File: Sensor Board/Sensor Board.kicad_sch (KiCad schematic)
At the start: 32 parts, among them J1 Programming Header, J3 Micro_SD_Card, U1 PIC18F26K83, U3 SPX3819M5-L-3-3, U4 MCP2562, Y1 12MHz Crystal

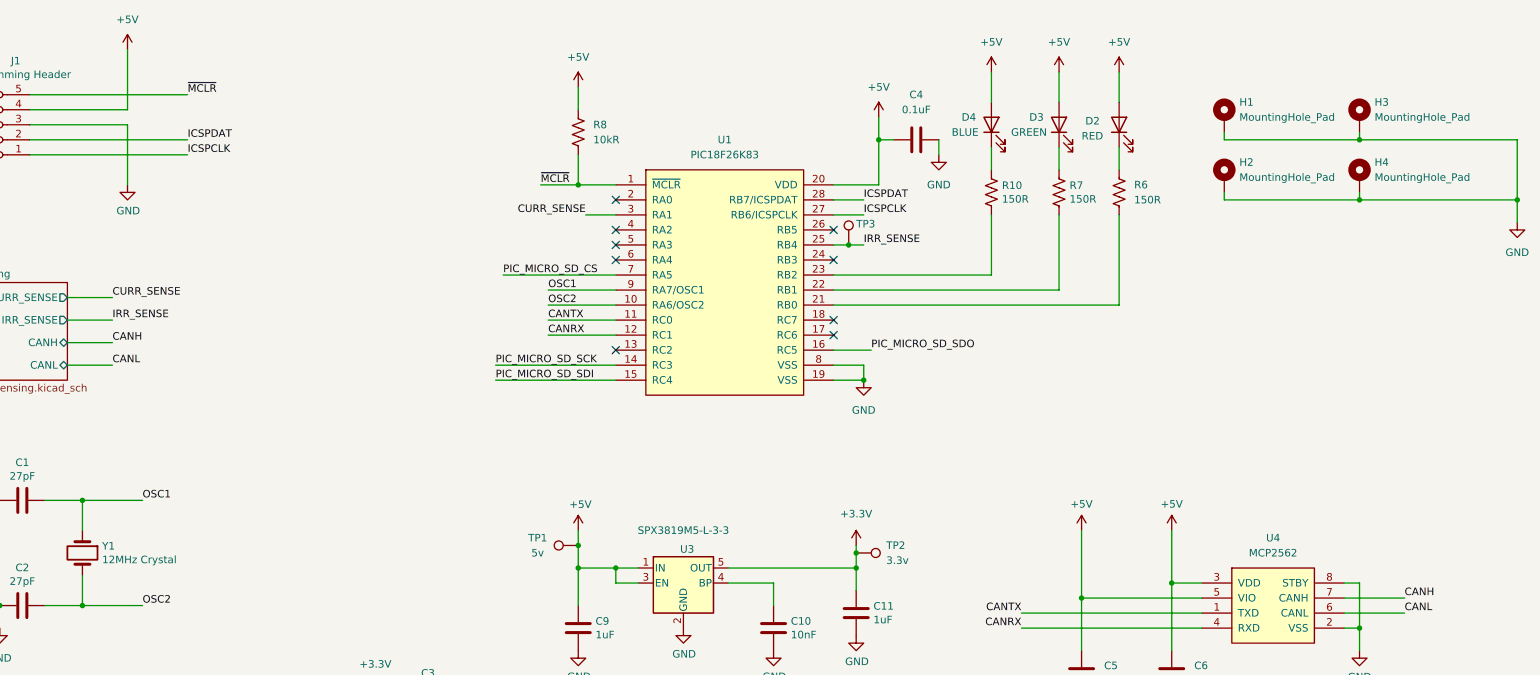
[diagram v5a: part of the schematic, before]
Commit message: Switch op amp
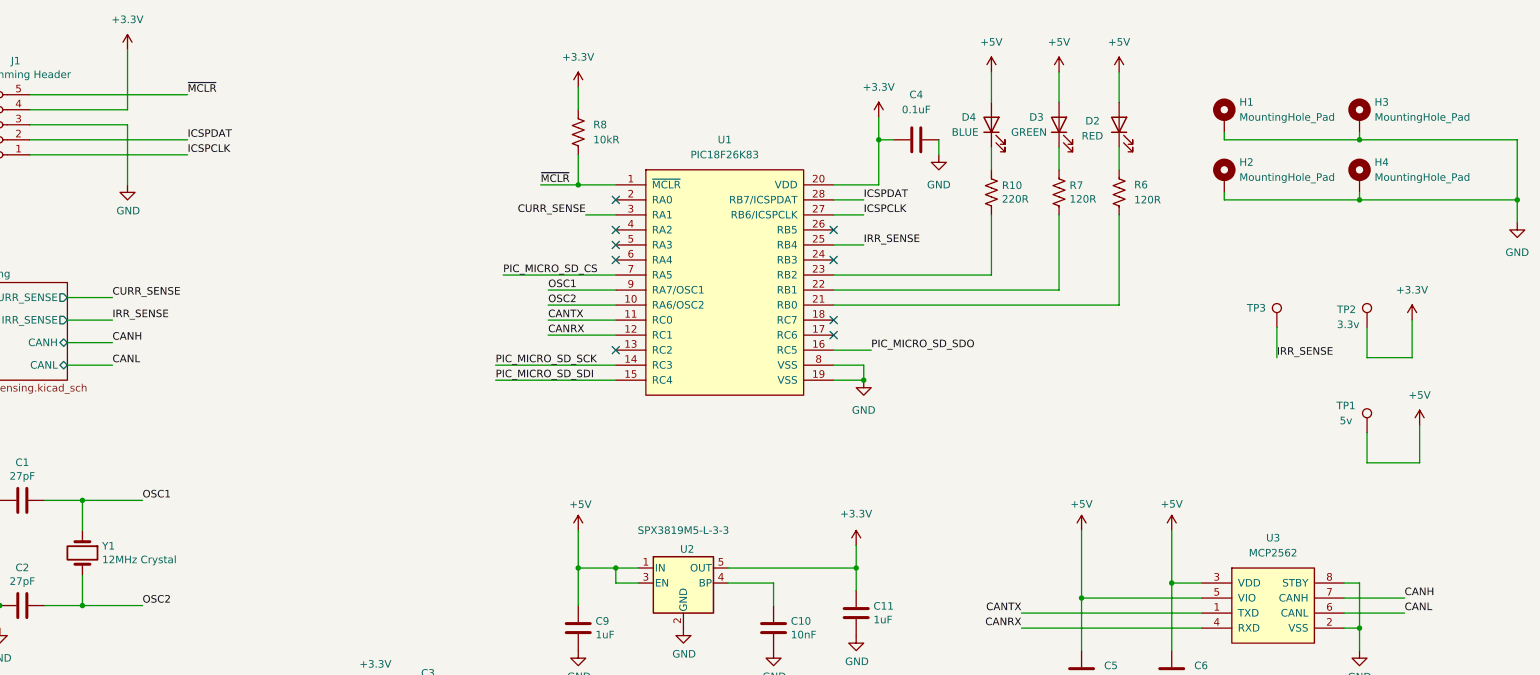
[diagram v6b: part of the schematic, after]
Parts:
- R10: value 150R -> 220R
- R6, R7: value 150R -> 120R
- U2: renamed from U3; footprint Package_TO_SOT_SMD:SOT-23-5 -> Package_TO_SOT_SMD:SOT-23-5_HandSoldering
- renumbered U4 to U3
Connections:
- net +3.3V: now also C4.1, J1.4 (Pin_4), R8.1, U1.20 (VDD)
- net +5V: no longer C4.1, J1.4 (Pin_4), R8.1, U1.20 (VDD)
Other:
- moved on the sheet: TP1, TP2, TP3

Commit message: Cooked another layout-Pranav
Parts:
- Y1: value 12MHz Crystal -> 12MHz Crystal
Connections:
- net CANRX: now also U1.25 (RB4); no longer U1.12 (RC1)
- net CANTX: now also U1.26 (RB5); no longer U1.11 (RC0)
- net CURR_SENSE: now also U1.4 (RA2); no longer U1.3 (RA1)
- net IRR_SENSE: now also U1.18 (RC7); no longer U1.25 (RB4)
- net PIC_MICRO_SD_CS: now also U1.21 (RB0); no longer U1.7 (RA5)
- net PIC_MICRO_SD_SCK: now also U1.23 (RB2); no longer U1.14 (RC3)
- net PIC_MICRO_SD_SDI: now also U1.24 (RB3); no longer U1.15 (RC4)
- net PIC_MICRO_SD_SDO: now also U1.22 (RB1); no longer U1.16 (RC5)
- net at U1.17 (RC6): now also R10.2
- net at R6.2: now also U1.15 (RC4); no longer U1.21 (RB0)
- net at R7.2: now also U1.16 (RC5); no longer U1.22 (RB1)
- no-connect marks 9 -> 8
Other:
- moved on the sheet: D2, R6
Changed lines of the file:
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@@
 	)
 	(no_connect
-		(at 162.56 73.66)
+		(at 125.73 78.74)
 	)
 	(no_connect
-		(at 125.73 60.96)
+		(at 125.73 53.34)
 	)
 	(no_connect
-		(at 162.56 71.12)
+		(at 125.73 60.96)
 	)
 	(no_connect
-		(at 125.73 50.8)
+		(at 125.73 73.66)
 	)
 	(no_connect
@@
 	)
 	(no_connect
-		(at 162.56 60.96)
-	)
-	(no_connect
-		(at 162.56 55.88)
+		(at 125.73 50.8)
 	)
 	(no_connect
@@
 	)
 	(no_connect
-		(at 125.73 55.88)
+		(at 125.73 71.12)
 	)
 	(wire
@@
 	(wire
 		(pts
-			(xy 200.66 29.21) (xy 200.66 34.29)
+			(xy 100.33 81.28) (xy 125.73 81.28)
 		)
 		(stroke
@@
 	(wire
 		(pts
-			(xy 120.65 53.34) (xy 125.73 53.34)
+			(xy 200.66 29.21) (xy 200.66 34.29)
 		)
 		(stroke
@@
 	(wire
 		(pts
-			(xy 210.82 29.21) (xy 210.82 34.29)
-		)
-		(stroke
-			(width 0)
-			(type default)
-		)
-	)
-	(wire
-		(pts
-			(xy 210.82 53.34) (xy 210.82 68.58)
+			(xy 100.33 27.94) (xy 100.33 33.02)
 		)
 		(stroke
@@
 	(wire
 		(pts
-			(xy 210.82 41.91) (xy 210.82 45.72)
+			(xy 100.33 40.64) (xy 100.33 44.45)
 		)
 		(stroke
@@
 	(wire
 		(pts
-			(xy 189.23 41.91) (xy 189.23 45.72)
+			(xy 200.66 53.34) (xy 200.66 76.2)
 		)
 		(stroke
@@
 	(wire
 		(pts
-			(xy 162.56 58.42) (xy 167.64 58.42)
+			(xy 189.23 41.91) (xy 189.23 45.72)
 		)
 		(stroke
@@
 	(wire
 		(pts
-			(xy 114.3 71.12) (xy 125.73 71.12)
-		)
-		(stroke
-			(width 0)
-			(type default)
-		)
-	)
-	(wire
-		(pts
 			(xy 85.09 134.62) (xy 85.09 138.43)
 		)
@@
 	(wire
 		(pts
-			(xy 162.56 66.04) (xy 200.66 66.04)
-		)
-		(stroke
-			(width 0)
-			(type default)
-		)
-	)
-	(wire
-		(pts
 			(xy 261.62 95.25) (xy 261.62 88.9)
 		)
@@
 	(wire
 		(pts
-			(xy 162.56 76.2) (xy 168.91 76.2)
-		)
-		(stroke
-			(width 0)
-			(type default)
-		)
-	)
-	(wire
-		(pts
 			(xy 125.73 115.57) (xy 125.73 113.03)
 		)
@@
 	(wire
 		(pts
-			(xy 105.41 81.28) (xy 125.73 81.28)
+			(xy 170.18 40.64) (xy 170.18 48.26)
 		)
 		(stroke
@@
 	(wire
 		(pts
-			(xy 170.18 40.64) (xy 170.18 48.26)
+			(xy 189.23 29.21) (xy 189.23 34.29)
 		)
 		(stroke
@@
 	(wire
 		(pts
-			(xy 189.23 29.21) (xy 189.23 34.29)
+			(xy 162.56 53.34) (xy 167.64 53.34)
 		)
 		(stroke
@@
 	(wire
 		(pts
-			(xy 162.56 53.34) (xy 167.64 53.34)
+			(xy 248.92 115.57) (xy 251.46 115.57)
 		)
 		(stroke
@@
 	(wire
 		(pts
-			(xy 248.92 115.57) (xy 251.46 115.57)
+			(xy 237.49 72.39) (xy 237.49 77.47)
 		)
 		(stroke
@@
 	(wire
 		(pts
-			(xy 237.49 72.39) (xy 237.49 77.47)
+			(xy 100.33 52.07) (xy 100.33 81.28)
 		)
 		(stroke
@@
 	(wire
 		(pts
-			(xy 200.66 53.34) (xy 200.66 66.04)
+			(xy 162.56 73.66) (xy 189.23 73.66)
 		)
 		(stroke
@@
 	(wire
 		(pts
-			(xy 189.23 53.34) (xy 189.23 63.5)
+			(xy 189.23 53.34) (xy 189.23 73.66)
 		)
 		(stroke
@@
 	(wire
 		(pts
-			(xy 114.3 73.66) (xy 125.73 73.66)
-		)
-		(stroke
-			(width 0)
-			(type default)
-		)
-	)
-	(wire
-		(pts
 			(xy 200.66 45.72) (xy 200.66 41.91)
 		)
@@
 	(wire
 		(pts
-			(xy 105.41 78.74) (xy 125.73 78.74)
-		)
-		(stroke
-			(width 0)
-			(type default)
-		)
-	)
-	(wire
-		(pts
 			(xy 144.78 113.03) (xy 166.37 113.03)
 		)
@@
 	(wire
 		(pts
-			(xy 21.59 119.38) (xy 21.59 123.19)
+			(xy 200.66 76.2) (xy 162.56 76.2)
 		)
 		(stroke
@@
 	(wire
 		(pts
-			(xy 172.72 40.64) (xy 170.18 40.64)
+			(xy 21.59 119.38) (xy 21.59 123.19)
 		)
 		(stroke
@@
 	(wire
 		(pts
-			(xy 106.68 63.5) (xy 125.73 63.5)
+			(xy 172.72 40.64) (xy 170.18 40.64)
 		)
 		(stroke
@@
 	(wire
 		(pts
-			(xy 162.56 68.58) (xy 210.82 68.58)
-		)
-		(stroke
-			(width 0)
-			(type default)
-		)
-	)
-	(wire
-		(pts
 			(xy 114.3 66.04) (xy 125.73 66.04)
 		)
@@
 	(wire
 		(pts
-			(xy 189.23 63.5) (xy 162.56 63.5)
-		)
-		(stroke
-			(width 0)
-			(type default)
-		)
-	)
-	(wire
-		(pts
 			(xy 48.26 181.61) (xy 48.26 161.29)
 		)
@@
 	)
 	(label "IRR_SENSE"
-		(at 167.64 58.42 0)
+		(at 162.56 71.12 0)
 		(fields_autoplaced yes)
 		(effects
@@
 	)
 	(label "CANTX"
-		(at 114.3 71.12 0)
+		(at 162.56 55.88 0)
 		(fields_autoplaced yes)
 		(effects
@@
 	)
 	(label "PIC_MICRO_SD_SCK"
-		(at 105.41 78.74 0)
+		(at 162.56 63.5 0)
 		(fields_autoplaced yes)
 		(effects
@@
 	)
 	(label "CANRX"
-		(at 114.3 73.66 0)
+		(at 162.56 58.42 0)
 		(fields_autoplaced yes)
 		(effects
@@
 	)
 	(label "PIC_MICRO_SD_SDO"
-		(at 168.91 76.2 0)
+		(at 162.56 66.04 0)
 		(fields_autoplaced yes)
 		(effects
@@
 	)
 	(label "PIC_MICRO_SD_SDI"
-		(at 105.41 81.28 0)
+		(at 162.56 60.96 0)
 		(fields_autoplaced yes)
 		(effects
@@
 	)
 	(label "PIC_MICRO_SD_CS"
-		(at 106.68 63.5 0)
+		(at 162.56 68.58 0)
 		(fields_autoplaced yes)
 		(effects
@@
 	)
 	(label "CURR_SENSE"
-		(at 120.65 53.34 180)
+		(at 125.73 55.88 180)
 		(fields_autoplaced yes)
 		(effects
@@
 			)
 		)
-		(property "Value" "12MHz Crystal "
+		(property "Value" "12MHz Crystal"
 			(at 38.8874 111.633 90)
 			(effects
@@
 		(lib_name "+5V_3")
 		(lib_id "power:+5V")
-		(at 210.82 29.21 0)
+		(at 100.33 27.94 0)
 		(unit 1)
 		(exclude_from_sim no)
@@
 		(fields_autoplaced yes)
 		(property "Reference" "#PWR06"
-			(at 210.82 33.02 0)
+			(at 100.33 31.75 0)
 			(effects
 				(font
@@
 		)
 		(property "Value" "+5V"
-			(at 210.82 24.13 0)
+			(at 100.33 22.86 0)
 			(effects
 				(font
@@
 		)
 		(property "Footprint" ""
-			(at 210.82 29.21 0)
+			(at 100.33 27.94 0)
 			(effects
 				(font
@@
 		)
 		(property "Datasheet" ""
-			(at 210.82 29.21 0)
+			(at 100.33 27.94 0)
 			(effects
 				(font
@@
 		)
 		(property "Description" "Power symbol creates a global label with name \"+5V\""
-			(at 210.82 29.21 0)
+			(at 100.33 27.94 0)
 			(effects
 				(font
@@
 	(symbol
 		(lib_id "Device:LED")
-		(at 210.82 38.1 90)
+		(at 100.33 36.83 90)
 		(unit 1)
 		(exclude_from_sim no)
@@
 		(dnp no)
 		(property "Reference" "D2"
-			(at 205.105 37.465 90)
+			(at 94.615 36.195 90)
 			(effects
 				(font
@@
 		)
 		(property "Value" "RED"
-			(at 204.47 40.005 90)
+			(at 93.98 38.735 90)
 			(effects
 				(font
@@
 		)
 		(property "Footprint" "LED_SMD:LED_1206_3216Metric_Pad1.42x1.75mm_HandSolder"
-			(at 210.82 38.1 0)
+			(at 100.33 36.83 0)
 			(effects
 				(font
@@
 		)
 		(property "Datasheet" "~"
-			(at 210.82 38.1 0)
+			(at 100.33 36.83 0)
 			(effects
 				(font
@@
 		)
 		(property "Description" ""
-			(at 210.82 38.1 0)
+			(at 100.33 36.83 0)
 			(effects
 				(font
@@
 		)
 		(property "DigiKey" "160-1457-1-ND"
-			(at 210.82 38.1 90)
+			(at 100.33 36.83 90)
 			(effects
 				(font
@@
 	(symbol
 		(lib_id "Device:R_US")
-		(at 210.82 49.53 0)
+		(at 100.33 48.26 0)
 		(unit 1)
 		(exclude_from_sim no)
@@
 		(fields_autoplaced yes)
 		(property "Reference" "R6"
-			(at 213.36 48.2599 0)
+			(at 102.87 46.9899 0)
 			(effects
 				(font
@@
 		)
 		(property "Value" "120R"
-			(at 213.36 50.7999 0)
+			(at 102.87 49.5299 0)
 			(effects
 				(font
@@
 		)
 		(property "Footprint" "Resistor_SMD:R_0805_2012Metric_Pad1.20x1.40mm_HandSolder"
-			(at 211.836 49.784 90)
+			(at 101.346 48.514 90)
 			(effects
 				(font
@@
 		)
 		(property "Datasheet" "~"
-			(at 210.82 49.53 0)
+			(at 100.33 48.26 0)
 			(effects
 				(font
@@
 		)
 		(property "Description" ""
-			(at 210.82 49.53 0)
+			(at 100.33 48.26 0)
 			(effects
 				(font
@@
 		)
 		(property "DigiKey" "738-RMCF0805FT160RCT-ND"
-			(at 210.82 49.53 0)
+			(at 100.33 48.26 0)
 			(effects
 				(font

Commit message: updated optics front end
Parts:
- removed C10: 10nF, Capacitor_SMD:C_0805_2012Metric_Pad1.18x1.45mm_HandSolder, symbol Device:C
- removed C11, C9: 1uF, Capacitor_SMD:C_0805_2012Metric_Pad1.18x1.45mm_HandSolder, symbol Device:C
- removed H1, H2, H3, H4: MountingHole_Pad, MountingHole:MountingHole_3.2mm_M3_DIN965_Pad, symbol Mechanical:MountingHole_Pad
- removed TP1: 5v, TestPoint:TestPoint_Pad_1.5x1.5mm, symbol Connector:TestPoint
- removed TP2: 3.3v, TestPoint:TestPoint_Pad_1.5x1.5mm, symbol Connector:TestPoint
- removed TP3: TestPoint, TestPoint:TestPoint_Pad_1.5x1.5mm, symbol Connector:TestPoint
- removed U2: SPX3819M5-L-3-3, Package_TO_SOT_SMD:SOT-23-5_HandSoldering, symbol Regulator_Linear:SPX3819M5-L-3-3
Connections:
- net +5V: no longer C5.2, U3.5 (VIO)
- net SCLK: now reaches U1.14 (RC3)
- net at R6.2: now also U1.5 (RA3); no longer U1.15 (RC4)
- net at R7.2: now also U1.6 (RA4); no longer U1.16 (RC5)
- net MCLKIN: now reaches U1.2 (RA0)
- net IRQ/MDAT: now reaches U1.3 (RA1)
- net CS: now reaches U1.7 (RA5)
- net +3.3V renamed +3V3D
- net +3V3D: now also C5.2, U3.5 (VIO)
- new net MISO: U1.16 (RC5)
- new net MOSI: U1.15 (RC4)
- no-connect marks 8 -> 3
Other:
- added sheet Power (Power.kicad_sch)
- sheet Sensing ports: added CS, IRQ/MDAT, MCLKIN, MISO, MOSI, SCLK; removed CANH, CANL, CURR_SENSE, IRR_SENSE
- moved on the sheet: C1, C2, C3, C4, C5, C6, D2, D3, D4, J1, J3, R10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
